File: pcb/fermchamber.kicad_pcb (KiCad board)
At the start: 2 copper layers, 149.5 x 129 mm, 41 parts, among them J1 12V IN, J2 DALLAS SENSOR, J3 5V OUT, J4 230 IN, J5 HEATER OUT, J6 HUMIDIFIER OUT, J7 BME280 SENSOR, K1 SANYOU_SRD_Form_C, Q2 IRLZ44N, Q3 NPN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

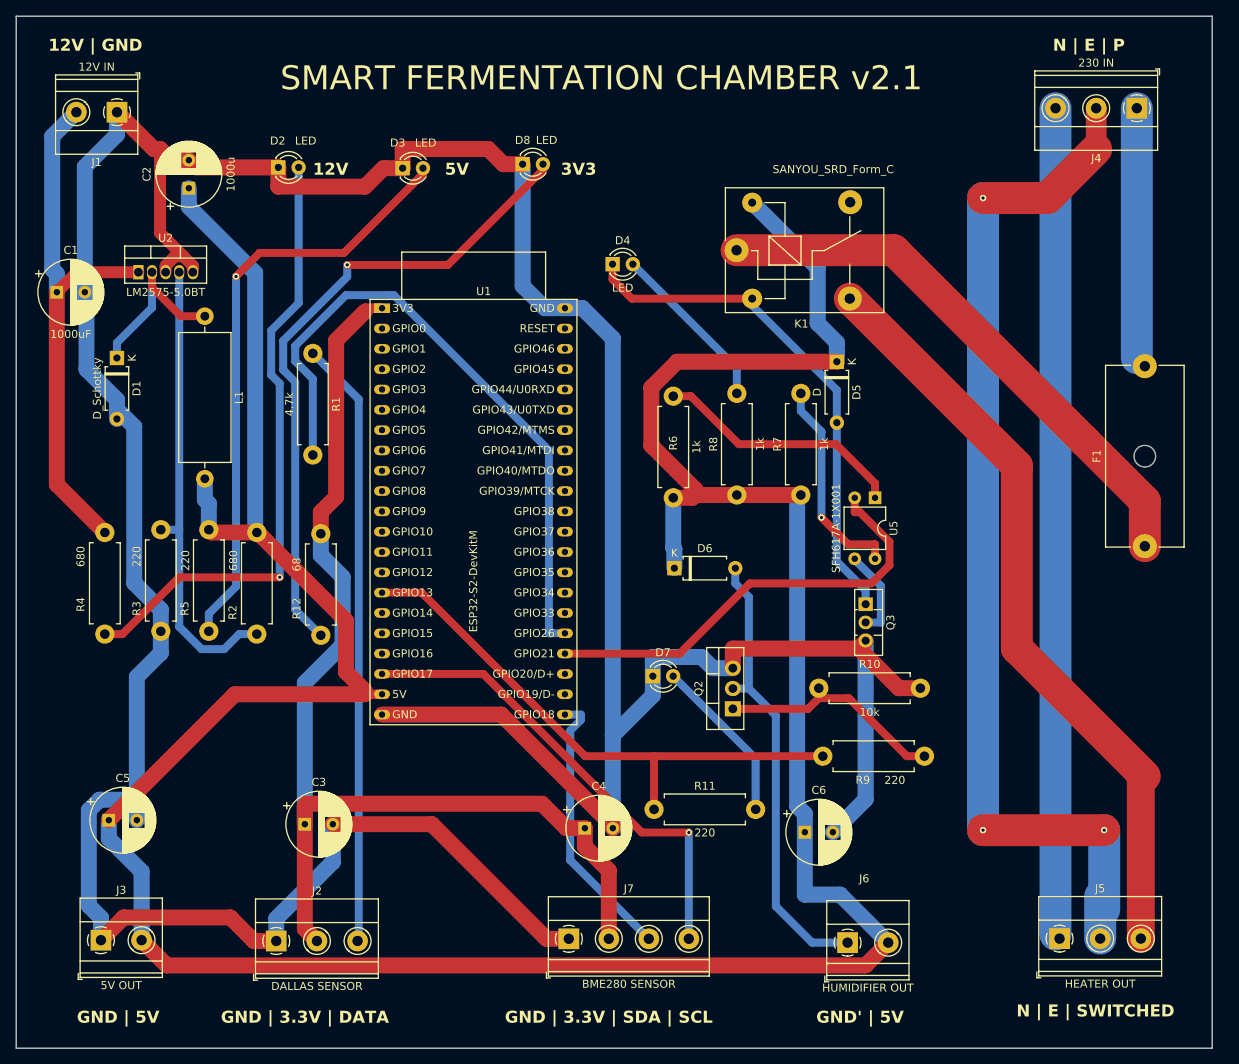
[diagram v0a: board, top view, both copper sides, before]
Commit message: fixed capactior, inductor and, voltage ic footprint in schematic; added missing labels on the pcb; clarified and added missing items in the BOM
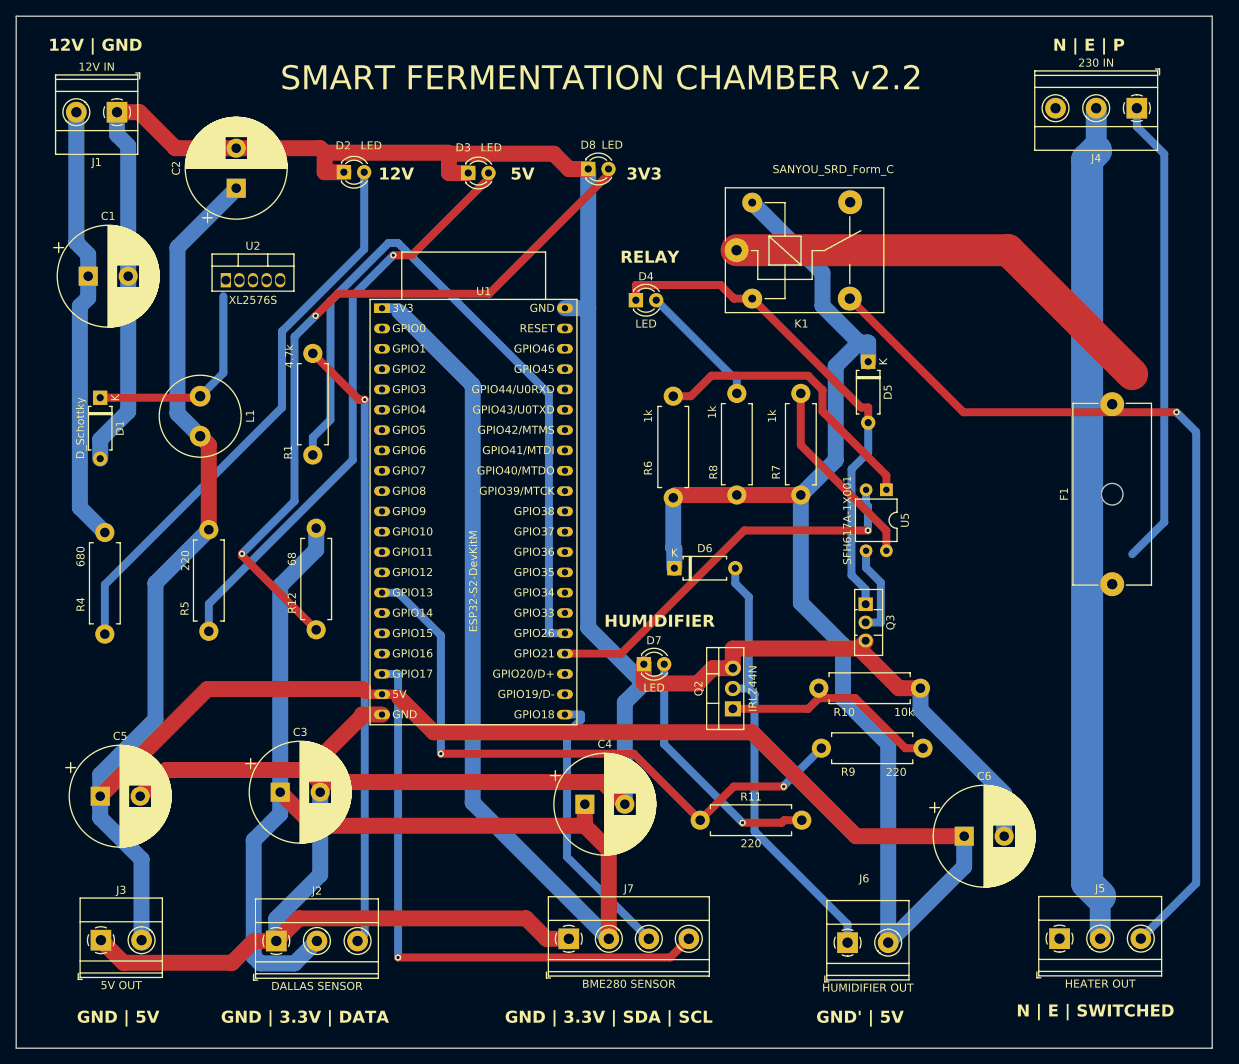
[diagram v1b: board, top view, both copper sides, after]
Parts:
- removed R2: 680, Resistor_THT:R_Axial_DIN0411_L9.9mm_D3.6mm_P12.70mm_Horizontal
- removed R3: 220, Resistor_THT:R_Axial_DIN0411_L9.9mm_D3.6mm_P12.70mm_Horizontal
- C1, C2, C3, C4, C5, C6: footprint Capacitor_THT:CP_Radial_D8.0mm_P3.50mm -> Capacitor_THT:CP_Radial_D12.5mm_P5.00mm
- L1: footprint Inductor_THT:L_Axial_L16.0mm_D6.3mm_P20.32mm_Horizontal_Fastron_VHBCC -> Inductor_THT:L_Radial_D10.0mm_P5.00mm_Fastron_07P
- U2: value LM2575-5.0BT -> XL2576S
- moved C6 19.9 mm to (143.5, 147.5)
- moved U2 11.0 mm to (51.2, 78.0)
- moved L1 10.0 mm to (48.0, 92.5)
- moved D2 8.22 mm to (66.0, 64.5)
- moved D3 8.22 mm to (81.5, 64.6)
- moved D8 8.22 mm to (96.5, 64.1)
- moved F1 6.26 mm to (162.0, 116.0)
- moved R11 5.92 mm to (110.5, 145.5)
- moved C2 5.92 mm to (52.5, 66.5)
- moved D1 5.39 mm to (35.5, 92.7)
- moved D4 5.36 mm to (102.5, 80.5)
- moved C3 5.05 mm to (58.0, 142.0)
- moved C1 4.40 mm to (34.0, 77.5)
- moved D5 3.92 mm to (131.5, 88.2)
- moved C5 3.19 mm to (35.5, 142.5)
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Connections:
- F1 pad 1: 230_P -> Net-(J4-Pin_1)
- J4 pad 1: 230_P -> Net-(J4-Pin_1)
- U2 pad 4: Net-(U2-FB) -> +5V
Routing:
- net 230_N: track 105.2 -> 0.00 mm
- net +3V3: track 140.9 -> 215.9 mm
- net Net-(J4-Pin_1): track 0.00 -> 58.8 mm
- net Net-(U2-FB): track 58.3 -> 0.00 mm
- net GND: track 480.6 -> 432.9 mm
- net 230_P: track 102.3 -> 55.9 mm
- net Earth_Protective: track 131.2 -> 104.9 mm, vias 3 -> 0
- net Net-(J5-Pin_3): track 95.5 -> 116.4 mm, vias 0 -> 1
- net Net-(J7-Pin_4): track 59.8 -> 74.8 mm
- net +12V: track 67.7 -> 54.9 mm
- net +5V: track 391.3 -> 379.4 mm
- net Net-(D7-A): track 20.9 -> 31.4 mm, vias 0 -> 1
- net Net-(D8-A): track 81.7 -> 91.5 mm, vias 1 -> 2
- net RELAY2_IN: track 70.2 -> 79.1 mm, vias 0 -> 2
- net Net-(U1-GPIO26): track 81.8 -> 90.2 mm
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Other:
- board text added: "HUMIDIFIER"
- board text added: "RELAY"
- board text added: "SMART FERMENTATION CHAMBER v2.2"
- board text removed: "SMART FERMENTATION CHAMBER v2.1"

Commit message: changed esp board to nodemcu 32s, limited current on leds, added diode for 5v usb programming backfeed, made switched labels more clear, fixed dallas data bus pull up, added pcb holes for mounting, removed unnecessary BOM items, removed relay optocoupler, re-routed pcb, fixed TODOs, added new render
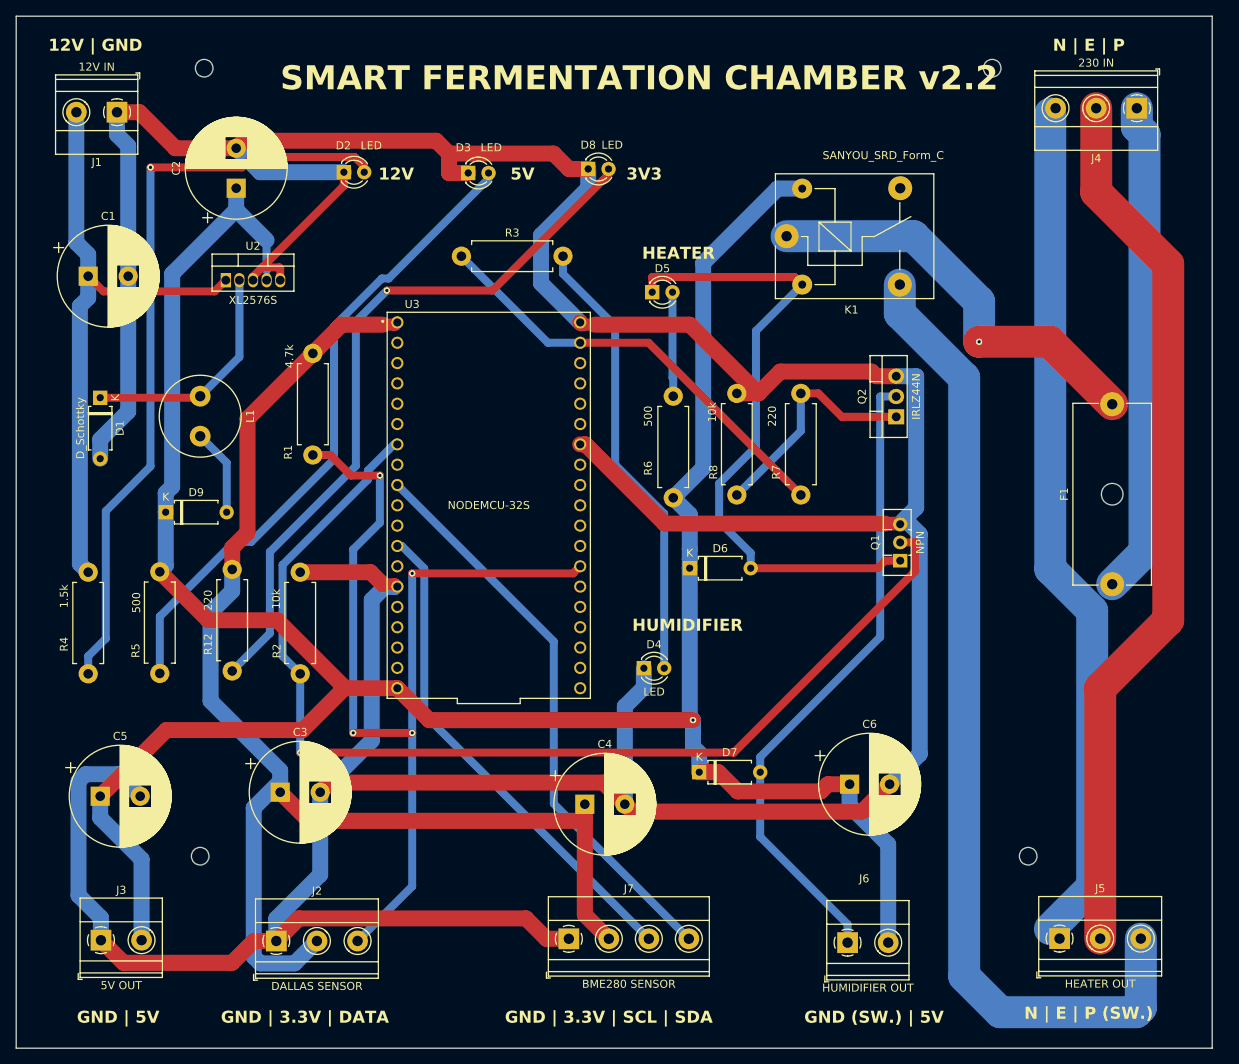
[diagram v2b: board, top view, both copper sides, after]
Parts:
- removed Q3: NPN, Package_TO_SOT_THT:TO-126-3_Vertical
- removed R10: 10k, Resistor_THT:R_Axial_DIN0411_L9.9mm_D3.6mm_P12.70mm_Horizontal
- removed R11, R9: 220, Resistor_THT:R_Axial_DIN0411_L9.9mm_D3.6mm_P12.70mm_Horizontal
- removed U1: ESP32-S2-DevKitM, PCM_Espressif:ESP32-S2-DevKitM
- removed U5: SFH617A-1X001, Package_DIP:DIP-4_W7.62mm
- added D9: D, Diode_THT:D_A-405_P7.62mm_Horizontal, F.Cu at (43.7, 107.0)
- added Q1: NPN, Package_TO_SOT_THT:TO-126-3_Vertical, F.Cu at (135.5, 113.1)
- added R2: 10k, Resistor_THT:R_Axial_DIN0411_L9.9mm_D3.6mm_P12.70mm_Horizontal, F.Cu at (60.5, 127.2)
- added R3: 220, Resistor_THT:R_Axial_DIN0411_L9.9mm_D3.6mm_P12.70mm_Horizontal, F.Cu at (80.7, 75.0)
- added REF**: MountingHole_2.2mm_M2, MountingHole:MountingHole_2.2mm_M2, F.Cu at (48.5, 51.5)
- added REF**: MountingHole_2.2mm_M2, MountingHole:MountingHole_2.2mm_M2, F.Cu at (151.5, 150.0)
- added REF**: MountingHole_2.2mm_M2, MountingHole:MountingHole_2.2mm_M2, F.Cu at (147.0, 51.5)
- added REF**: MountingHole_2.2mm_M2, MountingHole:MountingHole_2.2mm_M2, F.Cu at (48.0, 150.0)
- added U3: NODEMCU-32S, NodeMcuFootprint:MODULE_NODEMCU-32S, F.Cu at (84.1, 106.1)
- C1: value 1000uF -> 1000u
- D5: value D -> LED; footprint Diode_THT:D_A-405_P7.62mm_Horizontal -> LED_THT:LED_D3.0mm
- D7: value LED -> D; footprint LED_THT:LED_D3.0mm -> Diode_THT:D_A-405_P7.62mm_Horizontal
- R12: value 68 -> 220
- R4: value 680 -> 1.5k
- R5: value 220 -> 500
- R6: value 1k -> 500
- R7: value 1k -> 220
- R8: value 1k -> 10k
- moved D4 46.0 mm to (103.5, 126.5)
- moved Q2 41.8 mm to (135.0, 95.1)
- moved D5 28.4 mm to (104.5, 79.5), turned to 0 degrees
- moved C6 15.7 mm to (129.2, 141.0)
- moved D7 15.2 mm to (110.4, 139.5)
- moved R12 11.7 mm to (52.0, 126.8)
- moved R5 8.08 mm to (43.0, 114.5)
- moved K1 6.49 mm to (121.3, 72.5)
- moved R4 5.38 mm to (34.0, 114.5)
- moved D6 1.92 mm to (109.2, 114.0)
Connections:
- D4 pad 1: Net-(D4-K) -> GND
- D5 pad 1: +5V -> Net-(D5-K)
- D5 pad 2: Net-(D4-K) -> Net-(D5-A)
- D6 pad 2: Net-(D6-A) -> Net-(D5-K)
- D7 pad 1: GND -> +5V
- J2 pad 3: Net-(J2-Pin_3) -> PIN_DALLAS
- J6 pad 1: Net-(D6-A) -> Net-(D7-A)
- J7 pad 3: Net-(J7-Pin_3) -> BME_SCL
- J7 pad 4: Net-(J7-Pin_4) -> BME_SDA
- K1 pad 2: Net-(D4-K) -> Net-(D5-K)
- L1 pad 2: +5V -> Net-(D9-A)
- Q2 pad 2: Net-(D6-A) -> Net-(D7-A)
- R1 pad 1: Net-(J2-Pin_3) -> +3V3
- R1 pad 2: Net-(U1-GPIO26) -> PIN_DALLAS
- R6 pad 2: Net-(R6-Pad2) -> Net-(D5-A)
- R7 pad 1: +5V -> PIN_HUMIDIFIER
- R7 pad 2: Net-(R7-Pad2) -> Net-(Q2-G)
- R8 pad 1: +5V -> Net-(Q2-G)
- R8 pad 2: Net-(D4-A) -> GND
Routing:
- net GND: track 432.9 -> 572.0 mm
- net PIN_HEATER: track 0.00 -> 137.4 mm, vias 0 -> 1
- net PIN_DALLAS: track 0.00 -> 120.5 mm, vias 0 -> 4
- net 230_N: track 0.00 -> 108.9 mm
- net Net-(U1-GPIO26): track 90.2 -> 0.00 mm
- net Net-(D5-K): track 0.00 -> 81.5 mm
- net RELAY2_IN: track 79.1 -> 0.00 mm, vias 2 -> 0
- net Net-(J2-Pin_3): track 76.9 -> 0.00 mm, vias 1 -> 0
- net Net-(J7-Pin_4): track 74.8 -> 0.00 mm, vias 1 -> 0
- net BME_SDA: track 0.00 -> 71.8 mm
- net Net-(D4-K): track 63.5 -> 0.00 mm
- net +5V: track 379.4 -> 316.5 mm, vias 0 -> 1
- net BME_SCL: track 0.00 -> 62.5 mm
- net PIN_HUMIDIFIER: track 0.00 -> 54.8 mm
- net Net-(D6-A): track 54.6 -> 0.00 mm
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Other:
- board text added: "GND (SW.) | 5V"
- board text added: "GND | 3.3V | SCL | SDA"
- board text added: "HEATER"
- board text added: "N | E | P (SW.)"
- board text removed: "GND | 3.3V | SDA | SCL"
- board text removed: "GND' | 5V"
- board text removed: "N | E | SWITCHED"
- board text removed: "RELAY"
